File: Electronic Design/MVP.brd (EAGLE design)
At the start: 94.6 x 68.7 mm, 35 parts, among them IC1 ACS712ELC-5A, IC2 ATMEGA328-PU, Q1 IRF9540, Q2 IRF9540, X1 16MHz

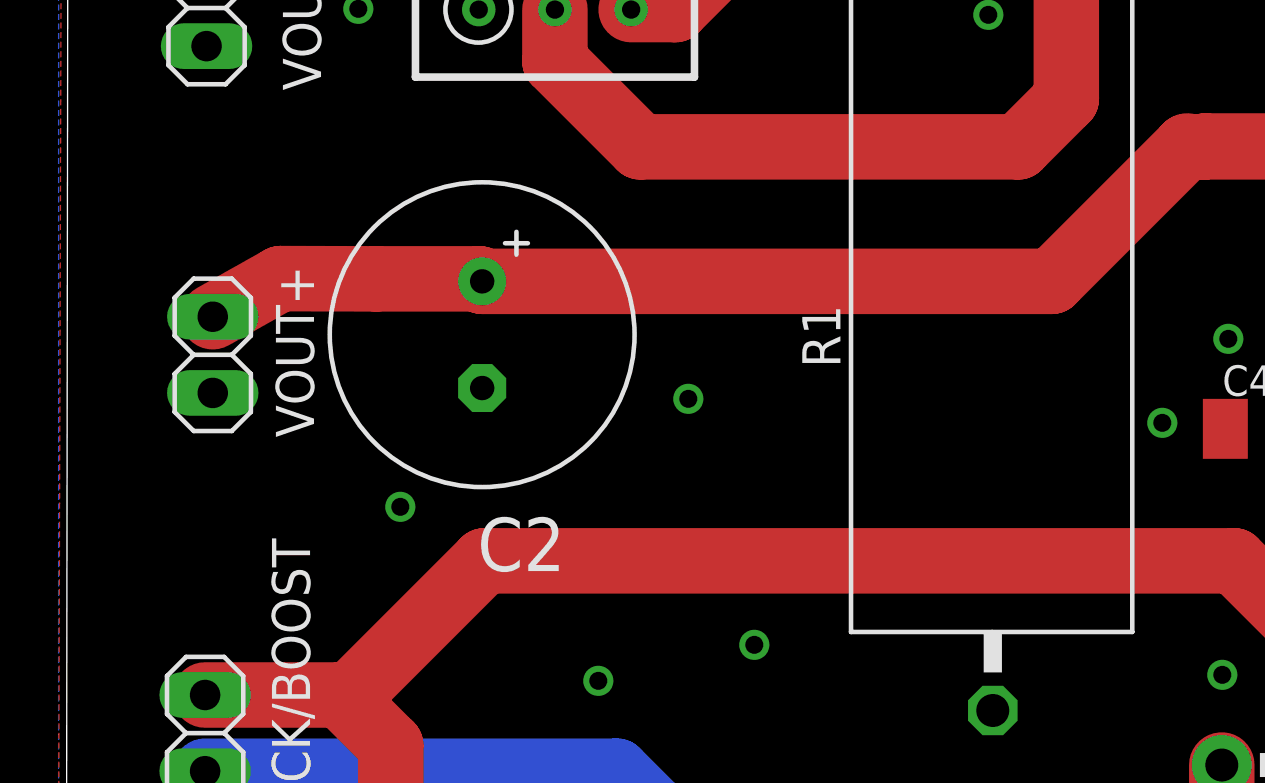
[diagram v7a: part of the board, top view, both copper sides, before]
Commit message: moved C2 into a more central position away from VOUT+ header
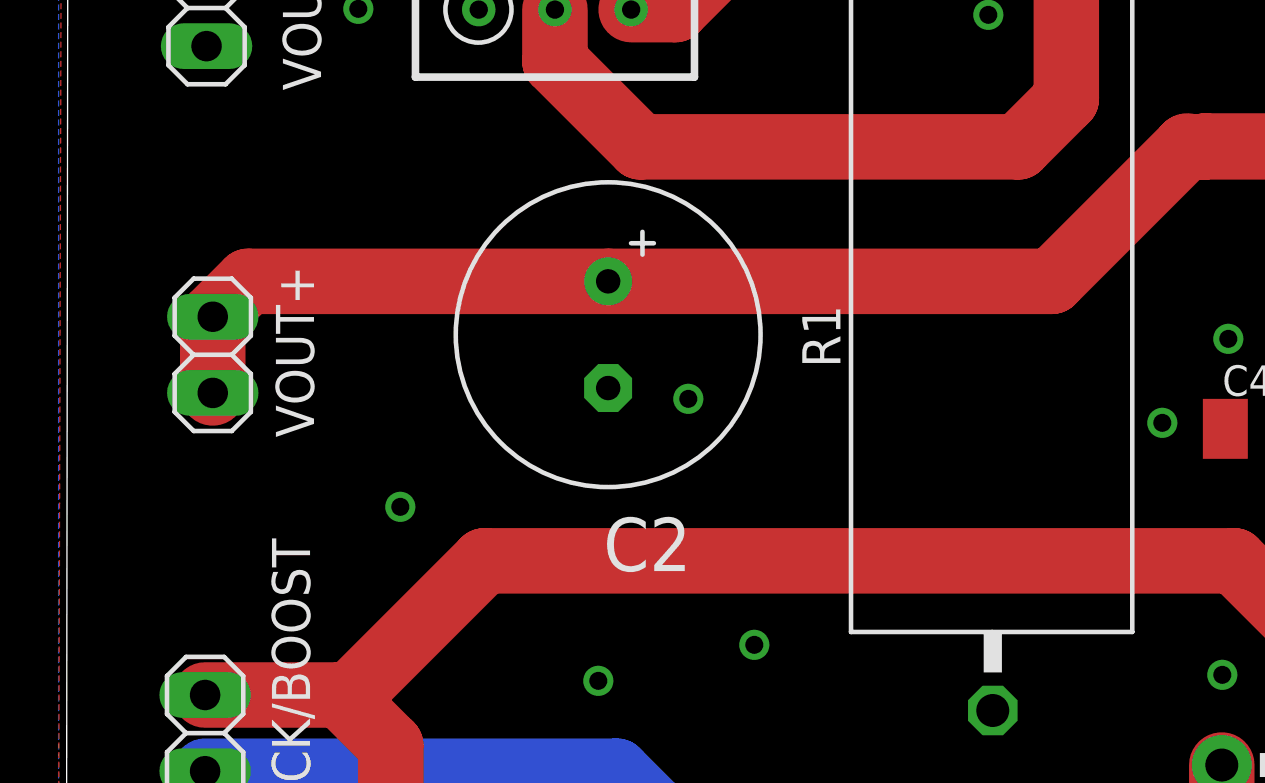
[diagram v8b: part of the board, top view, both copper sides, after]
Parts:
- moved C2 4.20 mm to (18.7, 43.3)
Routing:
- net M1S: track 43.6 -> 46.2 mm
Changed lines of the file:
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@@
 <attribute name="NAME" x="10.821571875" y="58.107325" size="1.778" layer="25" ratio="10"/>
 </element>
-<element name="C2" library="resistor" package="E3,5-10" value="ECA2DHG221" x="14.528428125" y="43.338675" smashed="yes" rot="R270">
-<attribute name="NAME" x="14.369428125" y="35.458675" size="1.778" layer="25" ratio="10"/>
-<attribute name="VALUE" x="16.661628125" y="50.282071875" size="1.778" layer="27" ratio="10" rot="R270"/>
+<element name="C2" library="resistor" package="E3,5-10" value="ECA2DHG221" x="18.728428125" y="43.338675" smashed="yes" rot="R270">
+<attribute name="NAME" x="18.569428125" y="35.458675" size="1.778" layer="25" ratio="10"/>
+<attribute name="VALUE" x="20.861628125" y="50.282071875" size="1.778" layer="27" ratio="10" rot="R270"/>
 </element>
 <element name="C1" library="resistor" package="C1206K" value="10n" x="55.990471875" y="43.541646875" smashed="yes" rot="R270">
@@
 <wire x1="43.3579625" y1="49.6281875" x2="42.8281875" y2="49.6281875" width="0.8128" layer="1"/>
 <wire x1="42.8281875" y1="49.6281875" x2="42.8" y2="49.6" width="0.8128" layer="1"/>
-<wire x1="5.548496875" y1="43.937340625" x2="7.807340625" y2="45.207340625" width="2.1844" layer="1"/>
-<wire x1="7.807340625" y1="45.207340625" x2="11" y2="45.2" width="2.1844" layer="1"/>
-<wire x1="11" y1="45.2" x2="14.445103125" y2="45.2" width="2.1844" layer="1"/>
-<wire x1="14.445103125" y1="45.2" x2="14.528428125" y2="45.116675" width="2.1844" layer="1"/>
-<wire x1="14.528428125" y1="45.116675" x2="33.516675" y2="45.116675" width="2.1844" layer="1"/>
 <contactref element="VOUT+" pad="2"/>
-<wire x1="5.548496875" y1="41.397340625" x2="5.548496875" y2="43.937340625" width="0" layer="19" extent="1-1"/>
+<wire x1="33.516675" y1="45.116675" x2="18.728428125" y2="45.116675" width="2.1844" layer="1"/>
+<wire x1="18.728428125" y1="45.116675" x2="6.72783125" y2="45.116675" width="2.1844" layer="1"/>
+<wire x1="6.72783125" y1="45.116675" x2="5.548496875" y2="43.937340625" width="2.1844" layer="1"/>
+<wire x1="5.548496875" y1="41.397340625" x2="5.548496875" y2="43.937340625" width="2.1844" layer="1"/>
 </signal>
 <signal name="N$3">
